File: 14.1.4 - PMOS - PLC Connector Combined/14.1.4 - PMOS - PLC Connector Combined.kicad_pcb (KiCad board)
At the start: 2 copper layers, 61.5 x 67.8 mm, 110 parts, among them J201 Conn_01x01_PAD, J202 Conn_01x01_PAD, J203 Conn_01x01_PAD, J204 Conn_01x01_PAD, J205 Conn_01x01_PAD, J206 Conn_01x01_PAD, J207 Conn_01x01_PAD, J208 Conn_01x01_PAD, J209 Conn_01x01_PAD, J210 Conn_01x01_PAD, J211 Conn_01x01_PAD, J212 Conn_01x01_PAD, J213 Conn_01x01_PAD, J214 Conn_01x01_PAD, J215 Conn_01x01_PAD, J216 Conn_01x01_PAD, J217 Conn_01x01_PAD, J218 Conn_01x01_PAD, J219 Conn_01x01_PAD, J220 Conn_01x01_PAD, J221 DB128L-5.08-2P-BK-S, J222 DB128L-5.08-2P-BK-S, J223 DB128L-5.08-2P-BK-S, J224 DB128L-5.08-2P-BK-S, J225 DB128L-5.08-2P-BK-S, J226 B04B-XASK-1, J301 Conn_01x01_PAD, J302 Conn_01x01_PAD, J303 Conn_01x01_PAD, J304 Conn_01x01_PAD, J305 Conn_01x01_PAD, J306 Conn_01x01_PAD, J307 Conn_01x01_PAD, J308 Conn_01x01_PAD, J309 Conn_01x01_PAD, J310 Conn_01x01_PAD, J311 Conn_01x01_PAD, J312 Conn_01x01_PAD, J313 Conn_01x01_PAD, J314 Conn_01x01_PAD, J315 Conn_01x01_PAD, J316 Conn_01x01_PAD, J317 DB128L-5.08-2P-BK-S, J318 DB128L-5.08-3P-BK-S, J319 DB128L-5.08-2P-BK-S, J320 DB128L-5.08-2P-BK-S, J321 B04B-XASK-1, Q1 2N7002, Q2 2N7002, Q3 2N7002, Q4 2N7002, U1 DMP6023LE-13, U2 DMP6023LE-13, U3 DMP6023LE-13, U4 DMP6023LE-13

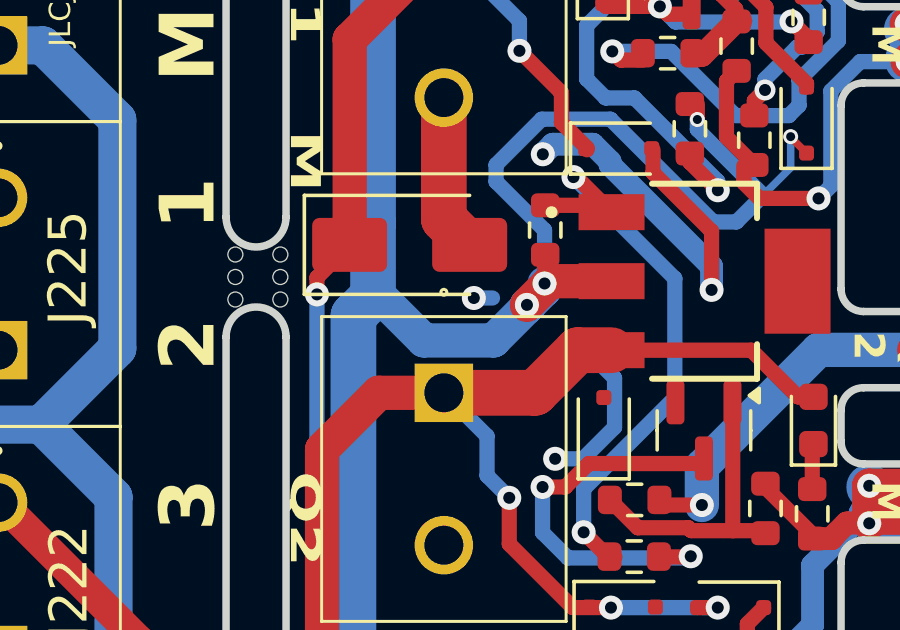
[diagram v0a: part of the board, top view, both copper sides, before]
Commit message: fixed non connected tracks
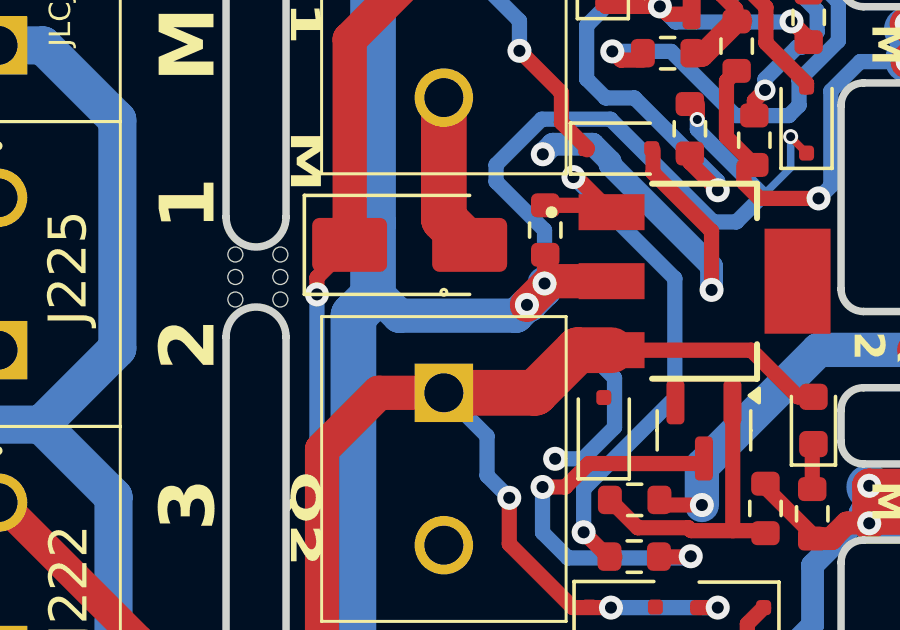
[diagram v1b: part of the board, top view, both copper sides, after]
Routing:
- net Net-(D10-K): track 142.9 -> 142.2 mm
- net GNDPWR: track 278.8 -> 278.1 mm, vias 29 -> 28
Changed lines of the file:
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@@
       (plotinvisibletext false)
       (sketchpadsonfab false)
-      (subtractmaskfromsilk false)
+      (subtractmaskfromsilk true)
       (outputformat 1)
       (mirror false)
@@
   (via (at 110.76 111.47) (size 0.8) (drill 0.4) (layers "F.Cu" "B.Cu") (free) (net 15))
   (via (at 123.88 76.7) (size 0.8) (drill 0.4) (layers "F.Cu" "B.Cu") (free) (net 15))
-  (via (at 108.5 85.84) (size 0.8) (drill 0.4) (layers "F.Cu" "B.Cu") (free) (net 15))
   (via (at 103.19 133.54) (size 0.8) (drill 0.4) (layers "F.Cu" "B.Cu") (free) (net 15))
   (via (at 122.93 76.7) (size 0.8) (drill 0.4) (layers "F.Cu" "B.Cu") (free) (net 15))
@@
   (segment (start 124.74851 123.13) (end 124.25 123.62851) (width 1.524) (layer "B.Cu") (net 15))
   (segment (start 128.23 92.65) (end 122.22851 92.65) (width 1.524) (layer "B.Cu") (net 15))
-  (segment (start 108.5 85.84) (end 109.122261 85.84) (width 0.508) (layer "B.Cu") (net 15))
   (segment (start 115.95 97.78) (end 118.76 97.78) (width 0.762) (layer "B.Cu") (net 15))
   (segment (start 112.14 87.46) (end 113.19 88.51) (width 0.508) (layer "B.Cu") (net 15))
@@
   (segment (start 105.31 111.490316) (end 105.31 101.1) (width 1.524) (layer "B.Cu") (net 33))
   (segment (start 110.51 100.86) (end 110.22 101.15) (width 1.524) (layer "B.Cu") (net 33))
-  (segment (start 110.27 86.142537) (end 109.159037 87.2535) (width 1.143) (layer "B.Cu") (net 33))
   (segment (start 105.31 99.480316) (end 105.31 101.1) (width 1.524) (layer "B.Cu") (net 33))
+  (segment (start 106.01 86.43) (end 105.14 85.56) (width 1.143) (layer "B.Cu") (net 33))
   (segment (start 113.055319 79.88) (end 110.76 79.88) (width 0.508) (layer "B.Cu") (net 33))
   (segment (start 110.76 79.88) (end 109.239931 81.400069) (width 0.508) (layer "B.Cu") (net 33))
@@
   (segment (start 110.37 104.62) (end 110.37 101) (width 0.508) (layer "B.Cu") (net 33))
   (segment (start 110.34 115.49) (end 109.309684 115.49) (width 1.524) (layer "B.Cu") (net 33))
+  (segment (start 105.14 85.56) (end 105.14 83.33) (width 1.143) (layer "B.Cu") (net 33))
+  (segment (start 110.27 86.07) (end 109.91 86.43) (width 1.143) (layer "B.Cu") (net 33))
   (segment (start 116.479319 83.304) (end 113.055319 79.88) (width 0.508) (layer "B.Cu") (net 33))
   (segment (start 109.239931 81.400069) (end 109.239931 81.962542) (width 0.508) (layer "B.Cu") (net 33))
@@
   (segment (start 104.486 86.430159) (end 104.486 98.656316) (width 1.524) (layer "B.Cu") (net 33))
   (segment (start 110.856624 85.555913) (end 110.342537 86.07) (width 1.143) (layer "B.Cu") (net 33))
-  (segment (start 110.27 86.07) (end 110.27 86.142537) (width 1.143) (layer "B.Cu") (net 33))
   (segment (start 108.524 101.15) (end 108.474 101.1) (width 1.524) (layer "B.Cu") (net 33))
   (segment (start 109.239931 81.962542) (end 110.856624 83.579235) (width 0.508) (layer "B.Cu") (net 33))
   (segment (start 105.14 71.36) (end 107.5 69) (width 1.524) (layer "B.Cu") (net 33))
   (segment (start 117.83113 118.75113) (end 116.44 117.36) (width 0.508) (layer "B.Cu") (net 33))
-  (segment (start 106.8335 87.2535) (end 105.14 85.56) (width 1.143) (layer "B.Cu") (net 33))
   (segment (start 104.486 98.656316) (end 105.31 99.480316) (width 1.524) (layer "B.Cu") (net 33))
+  (segment (start 109.91 86.43) (end 106.01 86.43) (width 1.143) (layer "B.Cu") (net 33))
   (segment (start 109.309684 115.49) (end 105.31 111.490316) (width 1.524) (layer "B.Cu") (net 33))
   (segment (start 110.856624 85.356624) (end 110.856624 85.555913) (width 1.143) (layer "B.Cu") (net 33))
@@
   (segment (start 110.37 101) (end 110.51 100.86) (width 0.508) (layer "B.Cu") (net 33))
   (segment (start 108.474 101.1) (end 105.31 101.1) (width 1.524) (layer "B.Cu") (net 33))
-  (segment (start 105.14 85.56) (end 105.14 83.33) (width 1.143) (layer "B.Cu") (net 33))
   (segment (start 116.44 117.36) (end 116.44 116.378737) (width 0.508) (layer "B.Cu") (net 33))
   (segment (start 110.342537 86.07) (end 110.27 86.07) (width 1.143) (layer "B.Cu") (net 33))
   (segment (start 119.060122 81.497617) (end 118.143306 82.414433) (width 0.25) (layer "B.Cu") (net 33))
   (segment (start 117.83113 118.80887) (end 117.88887 118.80887) (width 0.508) (layer "B.Cu") (net 33))
-  (segment (start 109.159037 87.2535) (end 106.8335 87.2535) (width 1.143) (layer "B.Cu") (net 33))
   (segment (start 110.856624 83.579235) (end 110.856624 85.356624) (width 0.508) (layer "B.Cu") (net 33))
   (segment (start 119.68 74.153735) (end 119.68 74.4375) (width 0.508) (layer "F.Cu") (net 34))

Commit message: 20241124
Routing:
- net Net-(R1-Pad1): track 26.7 -> 23.5 mm
- net GNDPWR: track 278.1 -> 278.9 mm
- net Net-(D10-K): track 142.2 -> 141.6 mm
